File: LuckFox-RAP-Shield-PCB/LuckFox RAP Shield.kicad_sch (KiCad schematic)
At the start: 5 parts, among them J1 LuckFox_Pico_Mini_SPI_Link, J2 DCJack_5.5x2.1mm+ReversePolar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, U2 W5500_Ethernet_Module_DNP_on_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, U3 MP1584EN_Buck_5V_3A

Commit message: Wire up LuckFox RAP Shield schematic manually in KiCad, remove onboard input-protection module
Manually drew the real wire connections in KiCad's schematic editor (the
previous commit only placed components + used global labels for
multi-endpoint power nets, per the connection table/wiring diagram --
this fills in the rest by hand in the GUI instead of scripted coordinates).

Also removed J2 (Input_Protection_DCJack_12V) -- reverse-polarity diode +
PTC fuse + TVS + DC jack now live on a separate external module instead of
on this shield, per a hardware decision to keep that circuitry off-board.
U3 (MP1584EN buck) is still present for now, fed by new +12V/-12V power
flags -- a follow-up commit removes it too once it's confirmed the buck
should also move off-board, replaced with a direct regulated-5V input
connector.

Checkpoint commit before further scripted edits, so manual GUI work here
has a safe revert point.
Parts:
- removed J2: DCJack_5.5x2.1mm+ReversePolarityDiode+PTCfuse3A+T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, symbol Breakout board symbols:Input_Protection_DCJack_12V
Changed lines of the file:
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@@
-	(wire
-		(pts
-			(xy 48.26 96.52) (xy 68.58 96.52)
-		)
-		(stroke
-			(width 0)
-			(type default)
-		)
-	)
 	(wire
 		(pts
@@
 	(wire
 		(pts
-			(xy 48.26 86.36) (xy 48.26 96.52)
-		)
-		(stroke
-			(width 0)
-			(type default)
-		)
-	)
-	(wire
-		(pts
 			(xy 223.52 163.83) (xy 223.52 139.7)
 		)
@@
 	(wire
 		(pts
-			(xy 107.84 91.44) (xy 157.76 91.44)
-		)
-		(stroke
-			(width 0)
-			(type default)
-		)
-	)
-	(wire
-		(pts
 			(xy 76.2 31.75) (xy 153.67 31.75)
 		)
@@
 	(wire
 		(pts
-			(xy 107.84 96.52) (xy 157.76 96.52)
-		)
-		(stroke
-			(width 0)
-			(type default)
-		)
-	)
-	(wire
-		(pts
 			(xy 127 39.37) (xy 127 139.7)
 		)
@@
 	(wire
 		(pts
-			(xy 39.37 91.44) (xy 68.58 91.44)
-		)
-		(stroke
-			(width 0)
-			(type default)
-		)
-	)
-	(wire
-		(pts
 			(xy 39.37 86.36) (xy 39.37 91.44)
 		)
@@
 	(wire
 		(pts
+			(xy 39.37 91.44) (xy 157.48 91.44)
+		)
+		(stroke
+			(width 0)
+			(type default)
+		)
+	)
+	(wire
+		(pts
 			(xy 166.37 166.37) (xy 166.37 129.54)
 		)
@@
 	(wire
 		(pts
+			(xy 48.26 96.52) (xy 48.26 86.36)
+		)
+		(stroke
+			(width 0)
+			(type default)
+		)
+	)
+	(wire
+		(pts
 			(xy 197.84 96.52) (xy 207.01 96.52)
 		)
@@
 		(pts
 			(xy 17.78 119.38) (xy 13.97 119.38)
+		)
+		(stroke
+			(width 0)
+			(type default)
+		)
+	)
+	(wire
+		(pts
+			(xy 48.26 96.52) (xy 157.48 96.52)
 		)
 		(stroke
@@
 					(unit 1)
 				)
-			)
-		)
-	)
-	(symbol
-		(lib_id "Breakout board symbols:Input_Protection_DCJack_12V")
-		(at 87.8 93.98 0)
-		(unit 1)
-		(body_style 1)
-		(exclude_from_sim no)
-		(in_bom yes)
-		(on_board yes)
-		(in_pos_files yes)
-		(dnp no)
-		(property "Reference" "J2"
-			(at 87.8 88.98 0)
-			(show_name no)
-			(do_not_autoplace no)
-			(effects
-				(font
-					(size 1.27 1.27)
-				)
-			)
-		)
-		(property "Value" "DCJack_5.5x2.1mm+ReversePolarityDiode+PTCfuse3A+TVS"
-			(at 87.8 91.48 0)
-			(show_name no)
-			(do_not_autoplace no)
-			(effects
-				(font
-					(size 1.27 1.27)
-				)
-			)
-		)
-		(property "Footprint" ""
-			(at 87.8 93.98 0)
-			(hide yes)
-			(show_name no)
-			(do_not_autoplace no)
-			(effects
-				(font
-					(size 1.27 1.27)
-				)
-			)
-		)
-		(property "Datasheet" ""
-			(at 87.8 93.98 0)
-			(hide yes)
-			(show_name no)
-			(do_not_autoplace no)
-			(effects
-				(font
-					(size 1.27 1.27)
-				)
-			)
-		)
-		(property "Description" ""
-			(at 87.8 93.98 0)
-			(show_name no)
-			(do_not_autoplace no)
-			(effects
-				(font
-					(size 1.27 1.27)
-				)
-			)
-		)
-		(pin "1"
-		)
-		(pin "2"
-		)
-		(pin "3"
-		)
-		(pin "4"
-		)
-		(instances
-			(project "LuckFox RAP Shield"
-				(path "/e63e39d7-6ac0-4ffd-8aa3-1841a4541b55"
-					(reference "J2")
-					(unit 1)
-				)

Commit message: Remove onboard buck converter (U3) from RAP Shield schematic
Power regulation (12V->5V buck) and reverse-polarity protection now
live on an external module ahead of the shield, not on the board
itself. U3 (MP1584EN) and its +12V/-12V power-flag symbols are
removed; a new 2-pin J2 connector (External_5V_Input_from_Buck_Module)
takes the shield's 5V input, positioned so its pins land exactly on
U3's old output-pin coordinates and reuse the existing downstream
wiring unchanged.
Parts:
- removed U3: MP1584EN_Buck_5V_3A, symbol Breakout board symbols:MP1584EN_Buck_12Vto5V_3A
- added J2: External_5V_Input_from_Buck_Module, symbol Breakout board symbols:External_5V_Input_from_Buck_Module
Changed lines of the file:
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@@
-	(wire
-		(pts
-			(xy 39.37 86.36) (xy 39.37 91.44)
-		)
-		(stroke
-			(width 0)
-			(type default)
-		)
-	)
 	(wire
 		(pts
@@
 	(wire
 		(pts
-			(xy 39.37 91.44) (xy 157.48 91.44)
-		)
-		(stroke
-			(width 0)
-			(type default)
-		)
-	)
-	(wire
-		(pts
 			(xy 166.37 166.37) (xy 166.37 129.54)
 		)
@@
 	(wire
 		(pts
-			(xy 48.26 96.52) (xy 48.26 86.36)
-		)
-		(stroke
-			(width 0)
-			(type default)
-		)
-	)
-	(wire
-		(pts
 			(xy 197.84 96.52) (xy 207.01 96.52)
 		)
@@
 		(pts
 			(xy 17.78 119.38) (xy 13.97 119.38)
-		)
-		(stroke
-			(width 0)
-			(type default)
-		)
-	)
-	(wire
-		(pts
-			(xy 48.26 96.52) (xy 157.48 96.52)
 		)
 		(stroke
@@
 	)
 	(symbol
-		(lib_id "Breakout board symbols:MP1584EN_Buck_12Vto5V_3A")
-		(at 177.8 93.98 0)
+		(lib_id "Breakout board symbols:External_5V_Input_from_Buck_Module")
+		(at 185.3 93.98 0)
 		(unit 1)
 		(body_style 1)
@@
 		(in_pos_files yes)
 		(dnp no)
-		(property "Reference" "U3"
-			(at 177.8 88.98 0)
-			(show_name no)
-			(do_not_autoplace no)
-			(effects
-				(font
-					(size 1.27 1.27)
-				)
-			)
-		)
-		(property "Value" "MP1584EN_Buck_5V_3A"
-			(at 177.8 91.48 0)
+		(property "Reference" "J2"
+			(at 185.3 85.09 0)
+			(show_name no)
+			(do_not_autoplace no)
+			(effects
+				(font
+					(size 1.27 1.27)
+				)
+			)
+		)
+		(property "Value" "External_5V_Input_from_Buck_Module"
+			(at 185.3 87.59 0)
 			(show_name no)
 			(do_not_autoplace no)
@@
 		)
 		(property "Footprint" ""
-			(at 177.8 93.98 0)
+			(at 185.3 93.98 0)
 			(hide yes)
 			(show_name no)
@@
 		)
 		(property "Datasheet" ""
-			(at 177.8 93.98 0)
+			(at 185.3 93.98 0)
 			(hide yes)
 			(show_name no)
@@
 		)
 		(property "Description" ""
-			(at 177.8 93.98 0)
-			(show_name no)
-			(do_not_autoplace no)
-			(effects
-				(font
-					(size 1.27 1.27)
-				)
-			)
+			(at 185.3 93.98 0)
+			(show_name no)
+			(do_not_autoplace no)
+			(effects
+				(font
+					(size 1.27 1.27)
+				)
+			)
+		)
+		(pin "1"
 		)
 		(pin "2"
-		)
-		(pin "3"
-		)
-		(pin "4"
-		)
-		(pin "1"
 		)
 		(instances
 			(project "LuckFox RAP Shield"
 				(path "/e63e39d7-6ac0-4ffd-8aa3-1841a4541b55"
-					(reference "U3")
-					(unit 1)
-				)
-			)
-		)
-	)
-	(symbol
-		(lib_id "power:+12V")
-		(at 39.37 86.36 0)
-		(unit 1)
-		(body_style 1)
-		(exclude_from_sim no)
-		(in_bom yes)
-		(on_board yes)
-		(in_pos_files yes)
-		(dnp no)
-		(fields_autoplaced yes)
-		(property "Reference" "#PWR01"
-			(at 39.37 90.17 0)
-			(hide yes)
-			(show_name no)
-			(do_not_autoplace no)
-			(effects
-				(font
-					(size 1.27 1.27)
-				)
-			)
-		)
-		(property "Value" "+12V"
-			(at 39.37 81.28 0)
-			(show_name no)
-			(do_not_autoplace no)
-			(effects
-				(font
-					(size 1.27 1.27)
-				)
-			)
-		)
-		(property "Footprint" ""
-			(at 39.37 86.36 0)
-			(hide yes)
-			(show_name no)
-			(do_not_autoplace no)
-			(effects
-				(font
-					(size 1.27 1.27)
-				)
-			)
-		)
-		(property "Datasheet" ""
-			(at 39.37 86.36 0)
-			(hide yes)
-			(show_name no)
-			(do_not_autoplace no)
-			(effects
-				(font
-					(size 1.27 1.27)
-				)
-			)
-		)
-		(property "Description" "Power symbol creates a global label with name \"+12V\""
-			(at 39.37 86.36 0)
-			(hide yes)
-			(show_name no)
-			(do_not_autoplace no)
-			(effects
-				(font
-					(size 1.27 1.27)
-				)
-			)
-		)
-		(pin "1"
-		)
-		(instances
-			(project "LuckFox RAP Shield"
-				(path "/e63e39d7-6ac0-4ffd-8aa3-1841a4541b55"
-					(reference "#PWR01")
+					(reference "J2")
 					(unit 1)
 				)
@@
 					(unit 1)
 				)
-			)
-		)
-	)
-	(symbol
-		(lib_id "power:-12V")
-		(at 48.26 86.36 0)
-		(unit 1)
-		(body_style 1)
-		(exclude_from_sim no)
-		(in_bom yes)
-		(on_board yes)
-		(in_pos_files yes)
-		(dnp no)
-		(fields_autoplaced yes)
-		(property "Reference" "#PWR02"
-			(at 48.26 90.17 0)
-			(hide yes)
-			(show_name no)
-			(do_not_autoplace no)
-			(effects
-				(font
-					(size 1.27 1.27)
-				)
-			)
-		)
-		(property "Value" "-12V"
-			(at 48.26 81.28 0)
-			(show_name no)
-			(do_not_autoplace no)
-			(effects
-				(font
-					(size 1.27 1.27)
-				)
-			)
-		)
-		(property "Footprint" ""
-			(at 48.26 86.36 0)
-			(hide yes)
-			(show_name no)
-			(do_not_autoplace no)
-			(effects
-				(font
-					(size 1.27 1.27)
-				)
-			)
-		)
-		(property "Datasheet" ""
-			(at 48.26 86.36 0)
-			(hide yes)
-			(show_name no)
-			(do_not_autoplace no)
-			(effects
-				(font
-					(size 1.27 1.27)
-				)
-			)
-		)
-		(property "Description" "Power symbol creates a global label with name \"-12V\""
-			(at 48.26 86.36 0)
-			(hide yes)
-			(show_name no)
-			(do_not_autoplace no)
-			(effects
-				(font
-					(size 1.27 1.27)
-				)
-			)
-		)
-		(pin "1"
-		)
-		(instances
-			(project "LuckFox RAP Shield"
-				(path "/e63e39d7-6ac0-4ffd-8aa3-1841a4541b55"
-					(reference "#PWR02")
-					(unit 1)
-				)

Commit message: Assign footprints to J1, J2, U2 so Update PCB from Schematic works
J1 (LuckFox link, 9 pins) and U2 (W5500 module, 8 pins) mount via
standard 2.54mm pin headers; J2 (external 5V input, 2 pins) is
hand-soldered wire but uses the same standard through-hole pad
footprint (a pin header with no header part actually populated) since
it's just plated holes sized for wire either way. All three reuse
KiCad's built-in Connector_PinHeader_2.54mm footprints rather than a
custom one, since there's no measured physical part to match.
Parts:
- J1: footprint (none) -> Connector_PinHeader_2.54mm:PinHeader_1x09_P2.54mm_Vertical
- J2: footprint (none) -> Connector_PinHeader_2.54mm:PinHeader_1x02_P2.54mm_Vertical
- U2: footprint (none) -> Connector_PinHeader_2.54mm:PinHeader_1x08_P2.54mm_Vertical
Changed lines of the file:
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@@
 			)
 		)
-		(property "Footprint" ""
+		(property "Footprint" "Connector_PinHeader_2.54mm:PinHeader_1x02_P2.54mm_Vertical"
 			(at 185.3 93.98 0)
 			(hide yes)
@@
 			)
 		)
-		(property "Footprint" ""
+		(property "Footprint" "Connector_PinHeader_2.54mm:PinHeader_1x08_P2.54mm_Vertical"
 			(at 242.57 134.62 0)
 			(hide yes)
@@
 			)
 		)
-		(property "Footprint" ""
+		(property "Footprint" "Connector_PinHeader_2.54mm:PinHeader_1x09_P2.54mm_Vertical"
 			(at 58.66 39.37 0)
 			(hide yes)

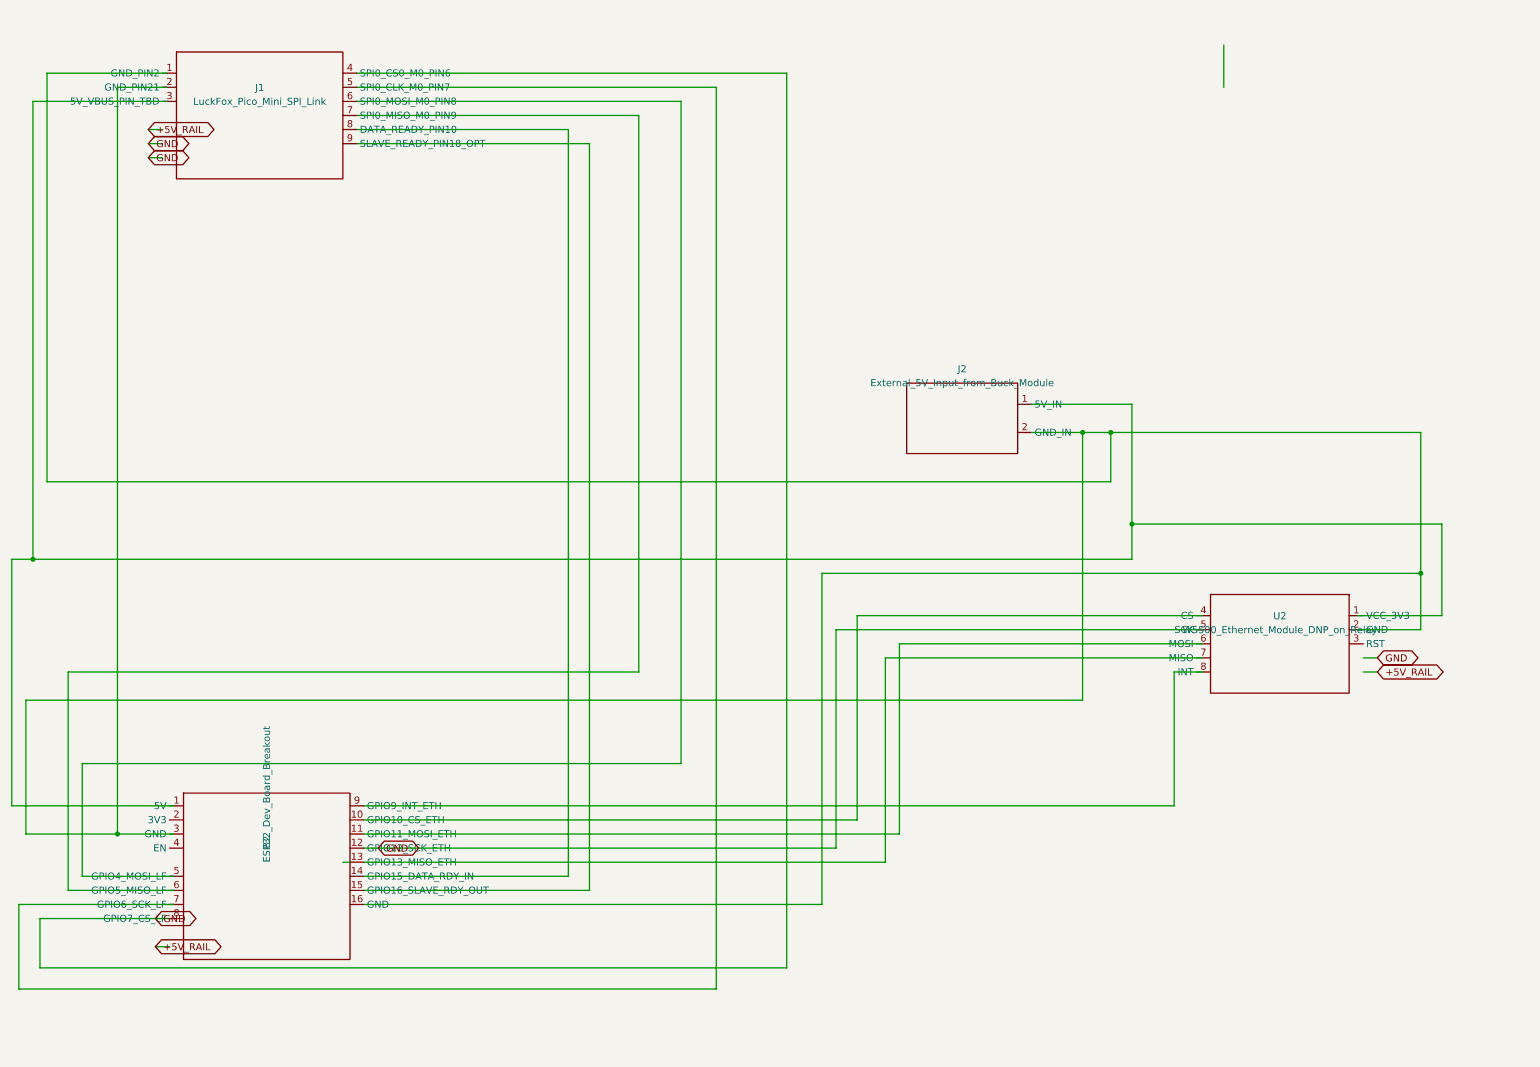
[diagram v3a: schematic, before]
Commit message: Rebuild J1 as real LuckFox Pico Mini 22-pin header, fix broken SPI wiring
J1 was a placeholder 9-pin symbolic connector for a cable link. LuckFox
is actually a Pi-HAT-style module plugging into a 2x11, 2.54mm-pitch
header (17.78mm row spacing, 21.00x28.14mm outline, per LuckFox's
official mechanical drawing). Rebuilt J1's schematic symbol with all
22 real pins/names, and added a matching custom footprint
(libs/footprints.pretty/LuckFox_Pico_Mini.kicad_mod) since no stock
KiCad footprint matches this pitch/spacing.

While rebuilding J1's wiring, traced the full netlist from the raw
wires/labels (not the wiring diagram) and found the existing manual
KiCad wiring was substantially broken: W5500's CS/SCK were tied to
+5V_RAIL/GND instead of the ESP32, the new J2 5V input was
miswired to an ESP32 SPI pin, and most of the LuckFox<->ESP32 SPI0
bus and ESP32<->W5500 SPI bus were simply dangling. Rewired the whole
signal/power netlist from scratch and verified every net
programmatically (union-find over wire/label endpoints against every
real component pin) before and after: SPI0 (LuckFox<->ESP32), SPI-ETH
(ESP32<->W5500), +5V_RAIL, +3V3_RAIL (also ties W5500 RST high), and
GND all now trace correctly with zero stray or dangling pins. Added
no_connect flags on the 13 LuckFox pins and ESP32's EN pin that are
intentionally unused.

Synced libs/symbols.kicad_sym and wiring_diagram.dot/.png to match.
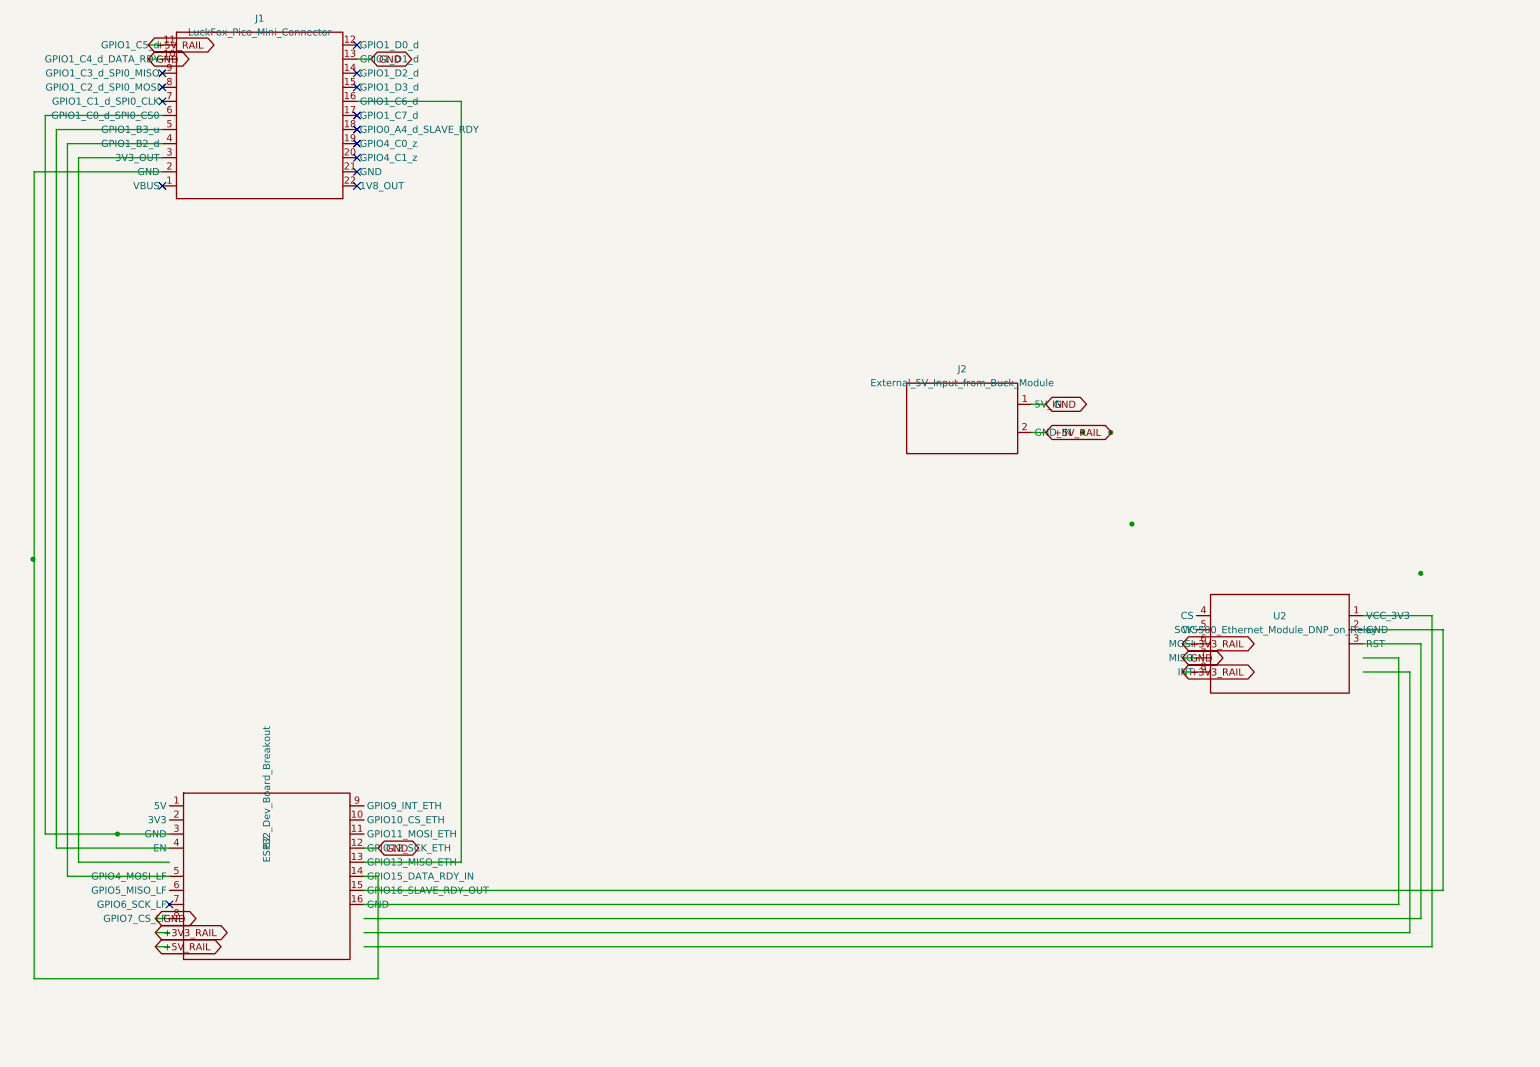
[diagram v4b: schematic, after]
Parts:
- J1: value LuckFox_Pico_Mini_SPI_Link -> LuckFox_Pico_Mini_Connector; footprint Connector_PinHeader_2.54mm:PinHeader_1x09_P2.54mm_Vertical -> footprints:LuckFox_Pico_Mini
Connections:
- no-connect marks 0 -> 14
